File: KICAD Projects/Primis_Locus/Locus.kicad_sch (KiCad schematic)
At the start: 37 parts, among them IC1 LSM6DSV16XTR, IC2 QMC6309, J3 Conn_01x05_Pin, J4 USB_C_Receptacle_USB2.0_16P, U1 nRF52833_QDxx, U2 TLV70036_SOT23-5, Y2 Crystal_GND24

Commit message: Locus Progress
-Finished Locus schematics
-Started on Locus PCB layout
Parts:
- removed D1: WS2812B, LED_SMD:LED_WS2812B_PLCC4_5.0x5.0mm_P3.2mm, symbol LED:WS2812B
- removed J3: Conn_01x05_Pin, Connector_PinHeader_1.00mm:PinHeader_1x05_P1.00mm_Vertical, symbol Connector:Conn_01x05_Pin
- removed R8: 2R2, Resistor_SMD:R_0805_2012Metric, symbol Device:R
- added C14: 12pF, Capacitor_SMD:C_0805_2012Metric, symbol Device:C
- added C20: 4.7uF, Capacitor_SMD:C_0805_2012Metric, symbol Device:C
- added CN1: S2B-PH-SM4-TB_LF_SN, Connector_JST:JST_PH_S2B-PH-SM4-TB_1x02-1MP_P2.00mm_Horizontal, symbol primis2:S2B-PH-SM4-TB_LF_SN
- added D2: WS2812B-2020, LED_SMD:LED_WS2812B-2020_PLCC4_2.0x2.0mm, symbol LED:WS2812B-2020
- added J1: Conn_ARM_SWD_TagConnect_TC2030-NL, Connector:Tag-Connect_TC2030-IDC-NL_2x03_P1.27mm_Vertical, symbol Connector:Conn_ARM_SWD_TagConnect_TC2030-NL
- added R1, R2, R4: 4.7k, Resistor_SMD:R_0805_2012Metric, symbol Device:R
- added R10, R11, R5, R6: 10k, Resistor_SMD:R_0805_2012Metric, symbol Device:R
- added R7: 5.1k, Resistor_SMD:R_0805_2012Metric, symbol Device:R
- added U3: ANT3216LL00R2400A, Oscillator:Oscillator_SMD_Silicon_Labs_LGA-6_2.5x3.2mm_P1.25mm, symbol primis2:ANT3216LL00R2400A
- added U4: TP4056-42-ESOP8, Package_SO:SOIC-8-1EP_3.9x4.9mm_P1.27mm_EP2.41x3.3mm_ThermalVias, symbol Battery_Management:TP4056-42-ESOP8
- added Y1: 32.768kHz, Crystal:Crystal_SMD_3215-2Pin_3.2x1.5mm, symbol Device:Crystal
- C16: value 4.7K -> 12pF; footprint Capacitor_SMD:C_0603_1608Metric -> Capacitor_SMD:C_0805_2012Metric
- C18: value 4.7K -> 4.7uF; footprint Capacitor_SMD:C_0603_1608Metric -> Capacitor_SMD:C_0805_2012Metric
- IC1: footprint LSM6DSV16BXTR -> LSM6DSV16XTR:LSM6DSV16BXTR
- IC2: footprint QMC6309 -> QMC6309:QMC6309
- J4: footprint (none) -> Connector_USB:USB_C_Receptacle_HRO_TYPE-C-31-M-12
- R9: value 10k -> 5.1k
- Y2: value Crystal_GND24 -> 32MHz; footprint (none) -> Crystal:Crystal_SMD_Abracon_ABM8G-4Pin_3.2x2.5mm
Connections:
- net DEC4 is gone; now on net DEC4_6: U1.38 (DEC4)
- net DEC6 is gone; now on net DEC4_6: U1.26 (DEC6)
- net GND: now also C16.2, C18.2, IC1.1 (SDO/SA0), R9.1, C14.1, C20.2, CN1.2, D2.2 (VSS), J1.5 (GND), R11.2, R7.1, U4.1 (TEMP), U4.3 (GND), U4.9 (EPAD)
- net LED_IN: now also D2.3 (DIN)
- net LED_OUT: now also D2.1 (DOUT)
- net SCL: now also R1.2; no longer C16.2, IC2.A2 (SCL)
- net SDA: now also R2.2; no longer C18.2, IC2.B2 (SDA)
- net VBUS: now also C7.1, U1.10 (VBUS), C20.1, U4.4 (V_{CC}), U4.8 (CE); no longer C15.1, U2.1 (IN)
- net VDD_nRF: now also J1.1 (VCC), R1.1, R2.1, R4.1, R5.1, R6.1; no longer C16.1, C18.1
- net at C19.1, U2.5 (OUT): now also D2.4 (VDD)
- net at J4.A5 (CC1): now also R7.2
- net at J4.B5 (CC2): now also R9.2
- net at U1.16 (P0.18/~{RESET}): now also R10.2; no longer R9.2
- net INT: now reaches U1.14 (P0.15)
- net INT: now also IC1.4 (INT1)
- net at U1.19 (SWDIO): now also J1.2 (SWDIO)
- net at U1.2 (XL1/P0.00): now also C14.2, Y1.2
- net at U1.20 (SWDCLK): now also J1.4 (SWCLK)
- net at U1.3 (XL2/P0.01): now also C16.1, Y1.1
- net at U1.7 (P0.11): now also U4.7 (~{CHRG})
- net CS: now reaches IC1.12 (CS)
- net CS: now also R4.2
- net SDX: now reaches IC1.2 (SDX/AH1/QVAR1)
- net SDX: now also IC2.B2 (SDA), R5.2
- net SCX: now reaches IC1.3 (SCX/AH2/QVAR2)
- net SCX: now also IC2.A2 (SCL), R6.2
- net ANT: no longer names the net of L2.1
- net ANT: now also U3.1
- new net: R11.1, U4.2 (PROG)
- new net: J1.3 (~{RESET}), R10.1
- new net VDDH: C15.1, C18.1, CN1.1, U1.9 (VDDH), U2.1 (IN), U4.5 (BAT)
- no-connect marks 2 -> 20
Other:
- moved on the sheet: C5, C6, C7, L1, L2

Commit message: More Locus work
-Just a quick backup of newest work on Locus
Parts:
- removed CN1: S2B-PH-SM4-TB_LF_SN, Connector_JST:JST_PH_S2B-PH-SM4-TB_1x02-1MP_P2.00mm_Horizontal, symbol primis2:S2B-PH-SM4-TB_LF_SN
- removed U3: ANT3216LL00R2400A, Oscillator:Oscillator_SMD_Silicon_Labs_LGA-6_2.5x3.2mm_P1.25mm, symbol primis2:ANT3216LL00R2400A
- removed U4: TP4056-42-ESOP8, Package_SO:SOIC-8-1EP_3.9x4.9mm_P1.27mm_EP2.41x3.3mm_ThermalVias, symbol Battery_Management:TP4056-42-ESOP8
- added C21: 4.7uF, Capacitor_SMD:C_0805_2012Metric, symbol Device:C
- added D1: LED, LED_SMD:LED_0603_1608Metric, symbol Device:LED
- added L3: AN3216-245, primis2:AN3216-245, symbol primis2:AN3216-245
- added R12: 1k, Resistor_SMD:R_0805_2012Metric, symbol Device:R
- added U3: SM02B-GHS-TB_LF_SN, primis2:SM02B-GHS-TB_LF_SN, symbol primis2:SM02B-GHS-TB_LF_SN
- added U5: MCP73831T-2ATI_OT, primis2:MCP73831T-2ATI_OT, symbol primis2:MCP73831T-2ATI_OT
- R11: value 10k -> 8k
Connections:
- net GND: now also C21.1, U3.2, U5.2 (VSS)
- net VBUS: now also R12.2, U5.4 (VDD)
- net VDDH: now also C21.2, U3.1, U5.3 (VBAT)
- net at L2.1: now also L3.1 (RF/Feed/termination)
- net at R11.1: now also U5.5 (PROG)
- new net: D1.2 (A), R12.1
- new net: D1.1 (K), U5.1 (STAT)
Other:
- moved on the sheet: C20, R11

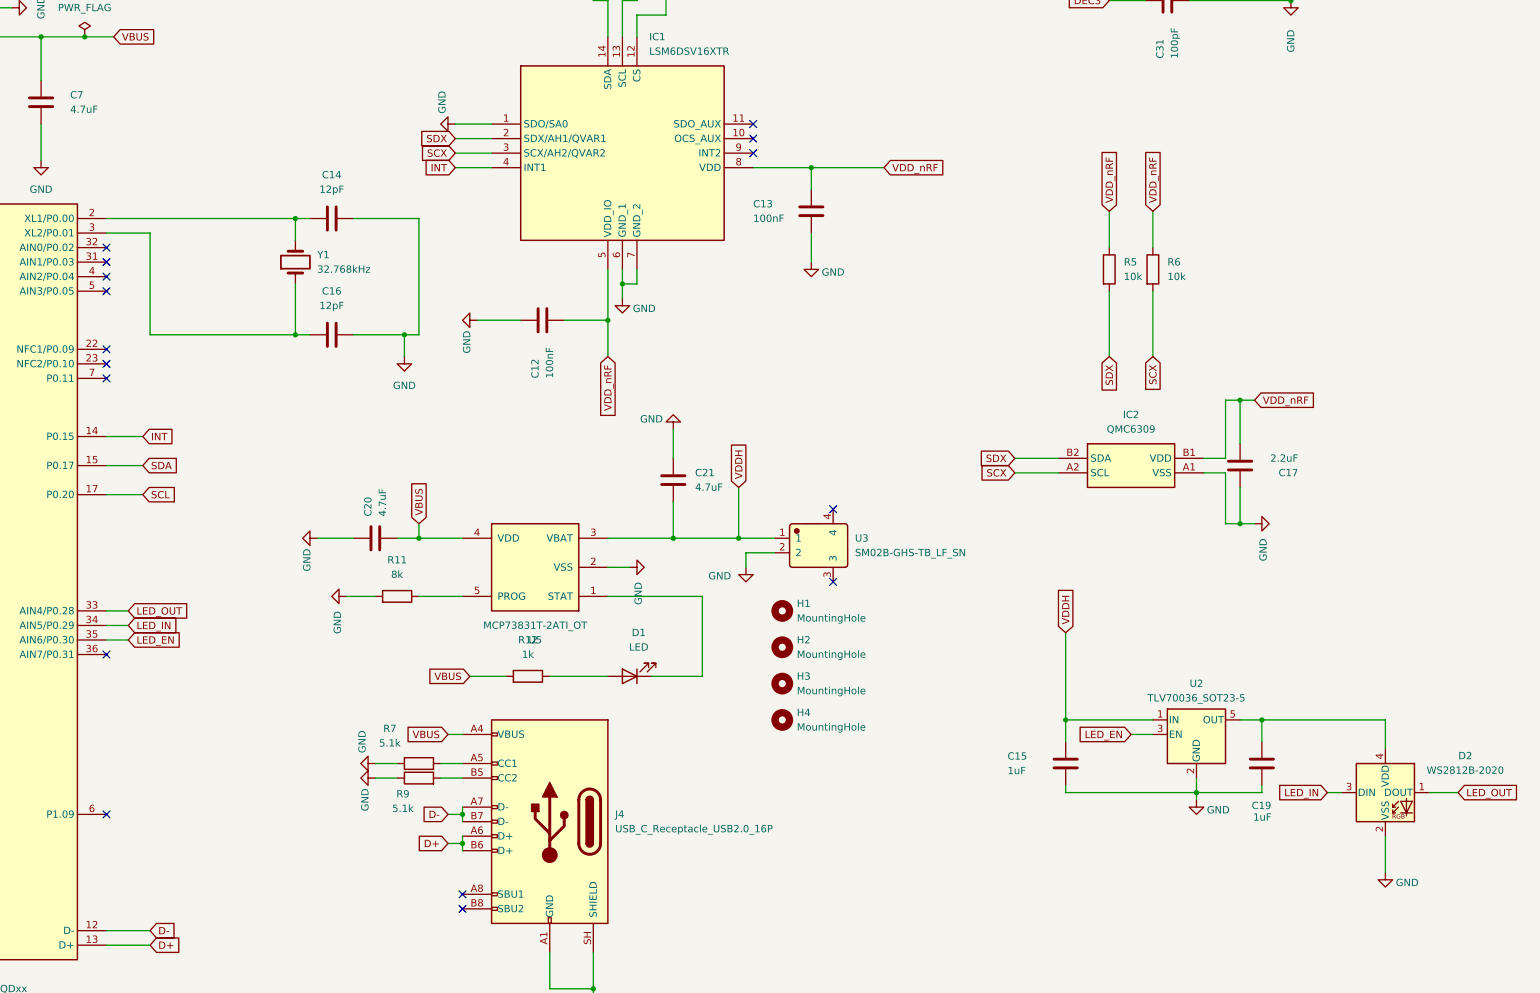
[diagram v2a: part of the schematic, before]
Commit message: Locus redesign + Some Models
-Locus now uses some 0402 parts
-Removed a bunch of unnecessary parts from Locus
-Shrunk the design down as a result
-Nearly finished routing Locus
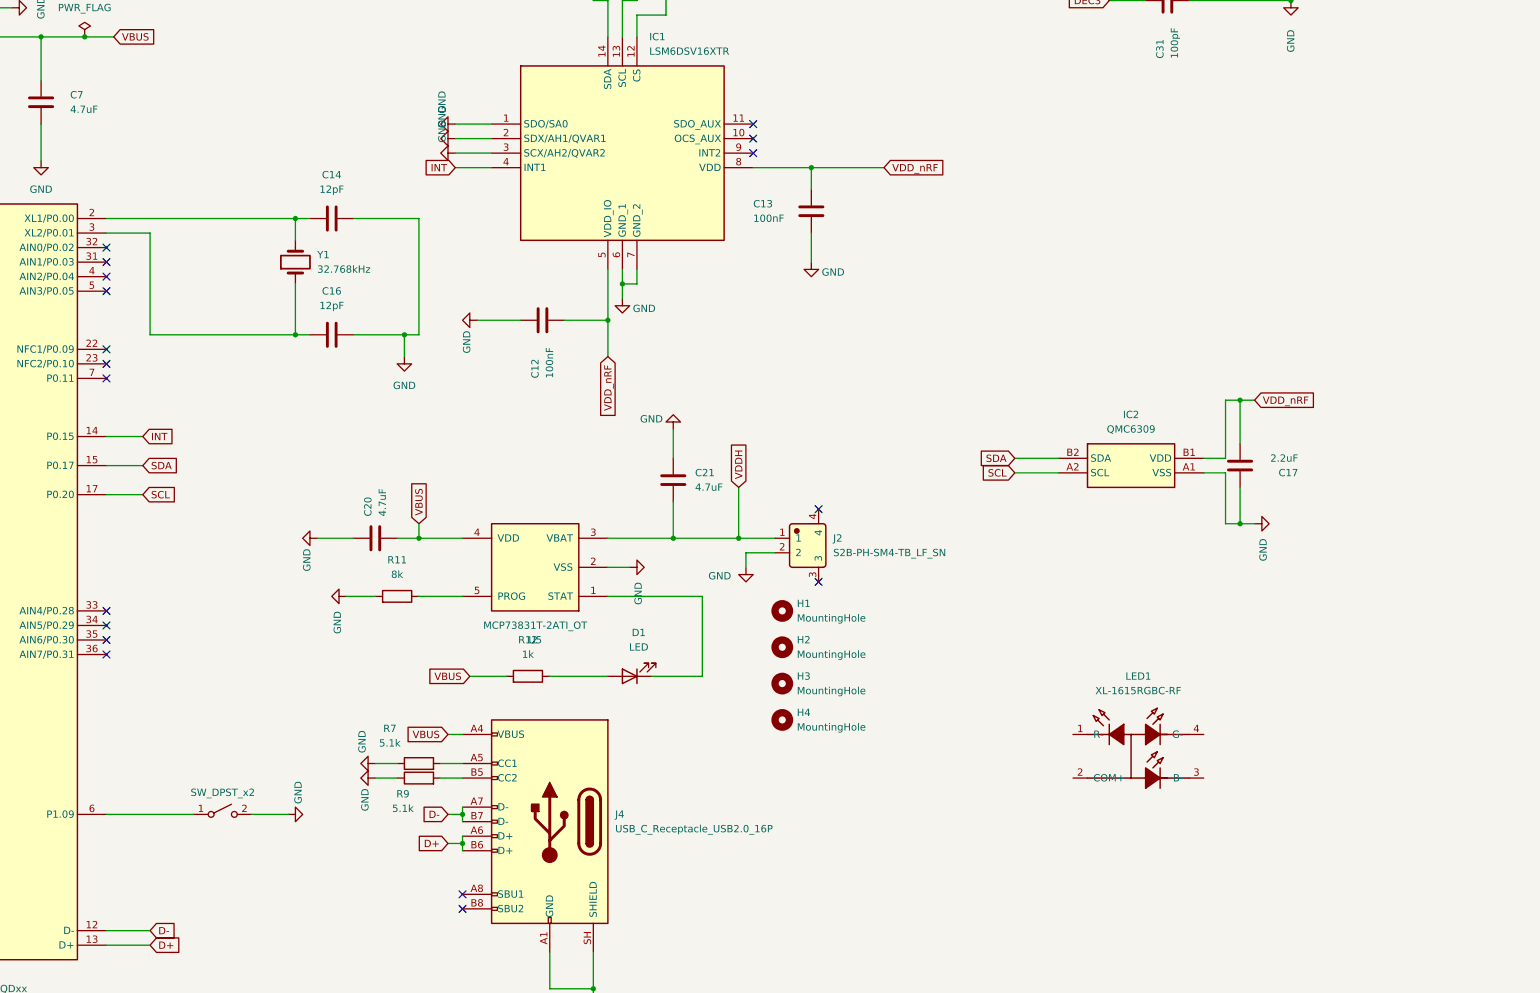
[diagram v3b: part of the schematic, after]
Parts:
- removed C15, C19: 1uF, Capacitor_SMD:C_0603_1608Metric, symbol Device:C
- removed D2: WS2812B-2020, LED_SMD:LED_WS2812B-2020_PLCC4_2.0x2.0mm, symbol LED:WS2812B-2020
- removed R5, R6: 10k, Resistor_SMD:R_0805_2012Metric, symbol Device:R
- removed U2: TLV70036_SOT23-5, Package_TO_SOT_SMD:SOT-23-5, symbol Regulator_Linear:TLV70036_SOT23-5
- removed U3: SM02B-GHS-TB_LF_SN, primis2:SM02B-GHS-TB_LF_SN, symbol primis2:SM02B-GHS-TB_LF_SN
- added J2: S2B-PH-SM4-TB_LF_SN, primis2:S2B-PH-SM4-TB_LF_SN, symbol primis2:S2B-PH-SM4-TB_LF_SN
- added LED1: XL-1615RGBC-RF, primis2:XL-1615RGBC-RF, symbol primis2:XL-1615RGBC-RF
- added SW1: SW_DPST_x2, primis2:SH-1806SA-A3DW-04, symbol Switch:SW_DPST_x2
- C1, C10, C12, C13, C30, C5, C6, C8: footprint Capacitor_SMD:C_0603_1608Metric -> Capacitor_SMD:C_0402_1005Metric
- C11, C14, C16, C29, C3, C31, C4: footprint Capacitor_SMD:C_0805_2012Metric -> Capacitor_SMD:C_0402_1005Metric
- C18, C2, C20, C21, C7, C9: footprint Capacitor_SMD:C_0805_2012Metric -> Capacitor_SMD:C_0603_1608Metric
- H1, H2, H3, H4: footprint MountingHole:MountingHole_2.2mm_M2 -> MountingHole:MountingHole_2.7mm_M2.5
- L1, L2: footprint Inductor_SMD:L_0603_1608Metric -> Inductor_SMD:L_0402_1005Metric
- R1, R10, R11, R12, R2, R4, R7, R9: footprint Resistor_SMD:R_0805_2012Metric -> Resistor_SMD:R_0402_1005Metric
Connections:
- net GND: now also IC1.2 (SDX/AH1/QVAR1), IC1.3 (SCX/AH2/QVAR2), J2.2, SW1.2 (B)
- net SCL: now also IC2.A2 (SCL)
- net SDA: now also IC2.B2 (SDA)
- net VDDH: now also J2.1
- net at U1.6 (P1.09): now also SW1.1 (A)
- net LED_EN: no longer names the net of U1.35 (AIN6/P0.30)
- net LED_IN: no longer names the net of U1.34 (AIN5/P0.29)
- net LED_OUT: no longer names the net of U1.33 (AIN4/P0.28)
- removed net SCX: IC1.3 (SCX/AH2/QVAR2), IC2.A2 (SCL)
- removed net SDX: IC1.2 (SDX/AH1/QVAR1), IC2.B2 (SDA)
- no-connect marks 20 -> 22

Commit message: Locus EV1 Final
-Finished Locus EV1
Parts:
- removed L3: AN3216-245, primis2:AN3216-245, symbol primis2:AN3216-245
- added L3, L5: N.C., Inductor_SMD:L_0402_1005Metric, symbol Device:L
- added L4: 2450AT18D0100001E, primis2:2450AT18D0100001E, symbol primis2:2450AT18D0100001E
- added R13: 82r, Resistor_SMD:R_0402_1005Metric, symbol Device:R
- added R14, R15: 33r, Resistor_SMD:R_0402_1005Metric, symbol Device:R
- added R16: 0r, Resistor_SMD:R_0402_1005Metric, symbol Device:R
- added TP1, TP2, TP3, TP4: TestPoint, TestPoint:TestPoint_Pad_1.0x1.0mm, symbol Connector:TestPoint
- R11: value 8k -> 5.6k
- renumbered LED1 to D2, IC1 to U2, IC2 to U3
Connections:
- net GND: now also L3.2, L4.2 (GND), L4.3 (GND), L4.4 (GND/FEED), L5.2, TP4.1
- net VBUS: now also TP3.1
- net VDDH: now also TP1.1
- net VDD_nRF: now also D2.2 (COM+), TP2.1
- net R: now reaches D2.1 (R-)
- net R: now also R13.1
- net B: now reaches D2.3 (B-)
- net B: now also R15.1
- net G: now reaches D2.4 (G-)
- net G: now also R14.1
- net at L2.1: now also L3.1, R16.2
- net at U1.33 (AIN4/P0.28): now also R13.2
- net at U1.34 (AIN5/P0.29): now also R14.2
- net at U1.35 (AIN6/P0.30): now also R15.2
- new net: L4.1 (FEED/GND), L5.1, R16.1
- no-connect marks 22 -> 18

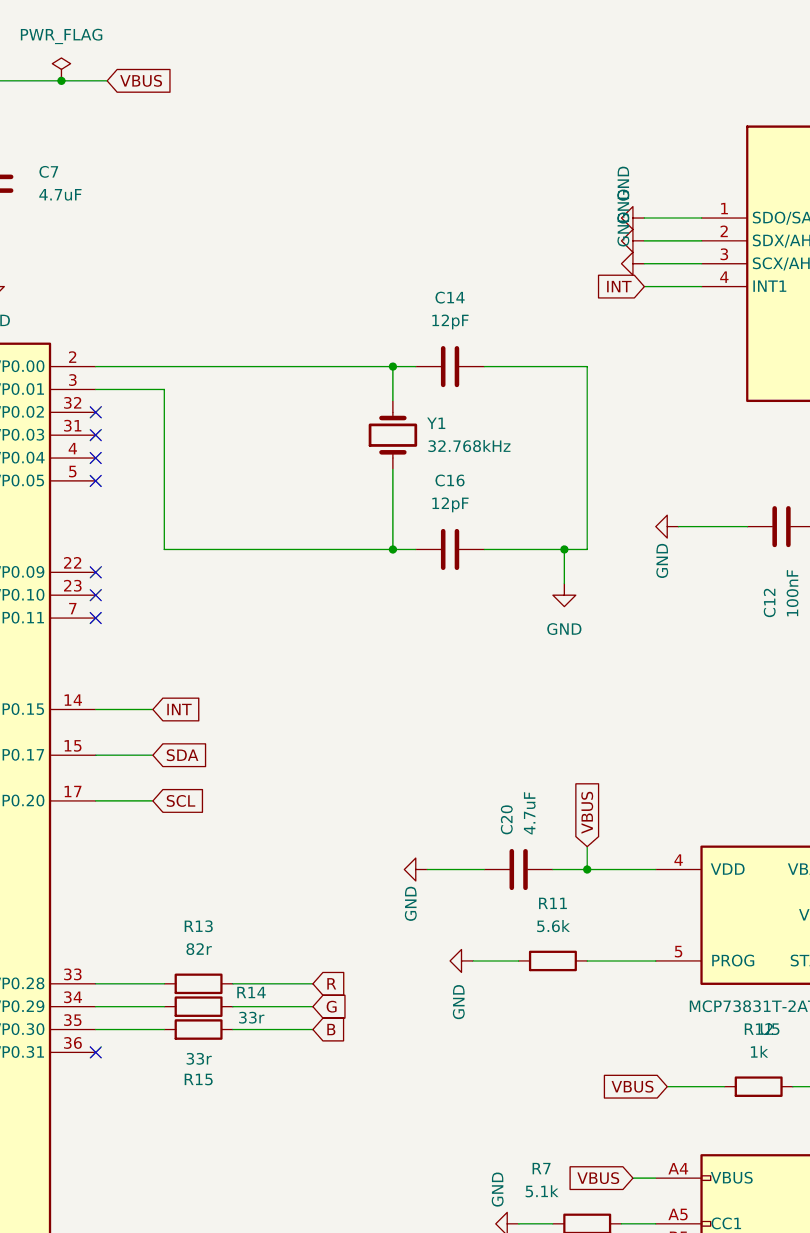
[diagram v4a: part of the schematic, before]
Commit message: Locus EV1 quick fixes
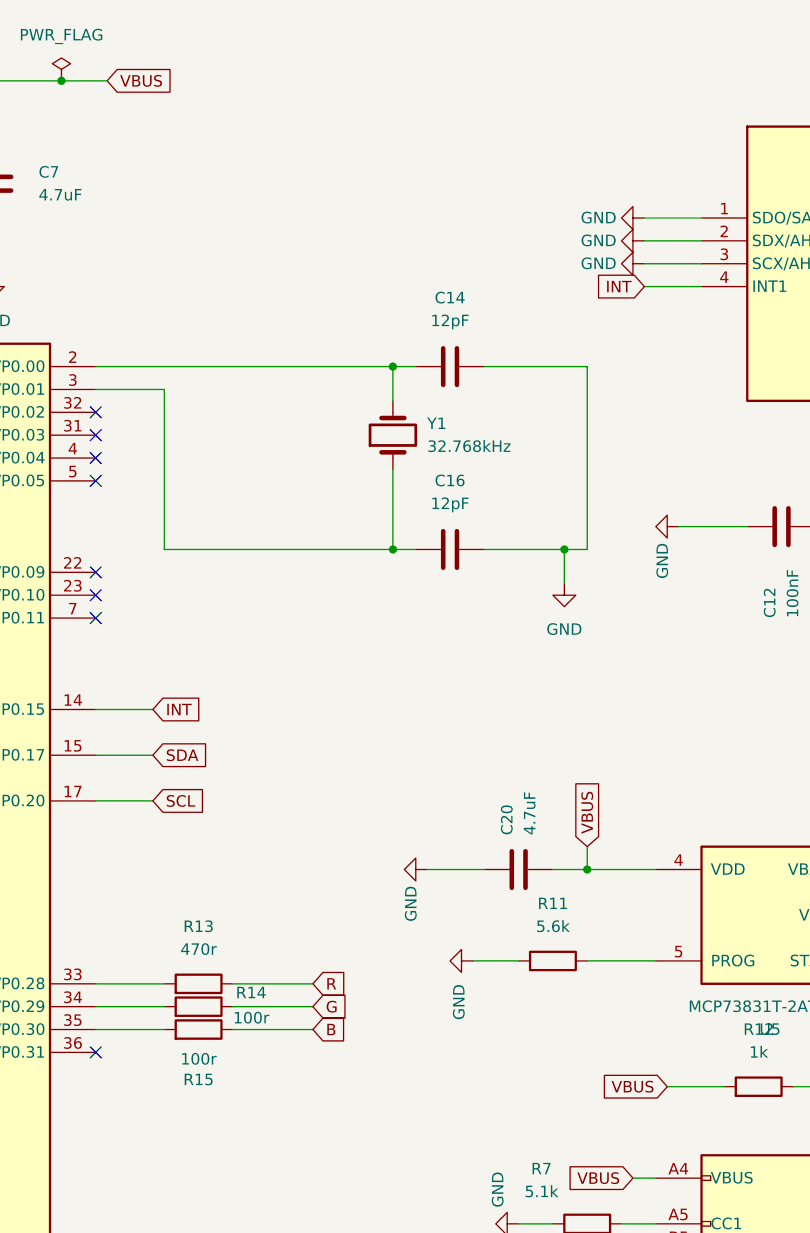
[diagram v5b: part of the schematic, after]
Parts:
- R13: value 82r -> 470r
- R14, R15: value 33r -> 100r
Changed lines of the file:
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@@
 		)
 		(property "Value" "GND"
-			(at 209.804 107.95 0)
+			(at 207.01 111.76 90)
 			(show_name no)
 			(do_not_autoplace no)
@@
 			)
 		)
-		(property "Value" "33r"
+		(property "Value" "100r"
 			(at 162.56 205.232 90)
 			(show_name no)
@@
 		)
 		(property "Value" "GND"
-			(at 209.804 113.03 0)
+			(at 207.01 116.84 90)
 			(show_name no)
 			(do_not_autoplace no)
@@
 			)
 		)
-		(property "Value" "33r"
+		(property "Value" "100r"
 			(at 168.402 200.66 90)
 			(show_name no)
@@
 			)
 		)
-		(property "Value" "82r"
+		(property "Value" "470r"
 			(at 162.56 193.04 90)
 			(show_name no)
@@
 		)
 		(property "Value" "GND"
-			(at 209.804 110.49 0)
+			(at 207.01 114.3 90)
 			(show_name no)
 			(do_not_autoplace no)

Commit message: Locus EV1 Crystal Fix
-One last crystal fixed, there good for real this time ordered
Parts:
- Y1: footprint Crystal:Crystal_SMD_3215-2Pin_3.2x1.5mm -> primis2:SC-20S32_768kHz20PPM9pF
- Y2: footprint Crystal:Crystal_SMD_Abracon_ABM8G-4Pin_3.2x2.5mm -> primis2:NX2016SA-32MHZ-STD-CZS-5
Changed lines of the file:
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@@
 			)
 		)
-		(property "Footprint" "Crystal:Crystal_SMD_Abracon_ABM8G-4Pin_3.2x2.5mm"
+		(property "Footprint" "primis2:NX2016SA-32MHZ-STD-CZS-5"
 			(at 48.26 193.04 0)
 			(hide yes)
@@
 			)
 		)
-		(property "Footprint" "Crystal:Crystal_SMD_3215-2Pin_3.2x1.5mm"
+		(property "Footprint" "primis2:SC-20S32_768kHz20PPM9pF"
 			(at 184.15 135.89 0)
 			(hide yes)
